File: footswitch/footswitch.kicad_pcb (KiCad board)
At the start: 2 copper layers, 100 x 50 mm, 65 parts, among them J1 control, Q1 TD9944, Q2 TD9944, Q3 TD9944, Q4 TD9944, SW1 SPST, SW2 SPST, SW3 SPST, U1 Teensy_LC, U2 74HC14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

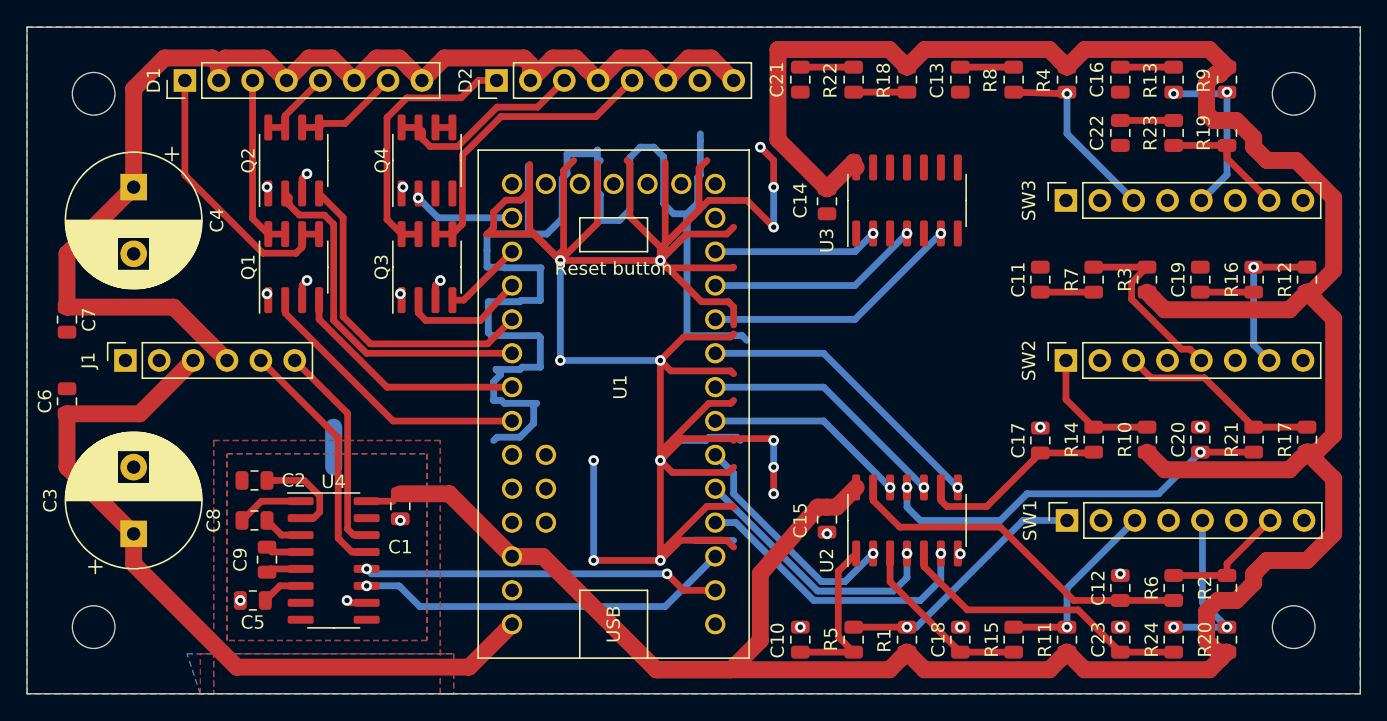
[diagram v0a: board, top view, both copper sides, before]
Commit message: Finalisation du PCB de la footswitch. Correction de la position des mounting holes.
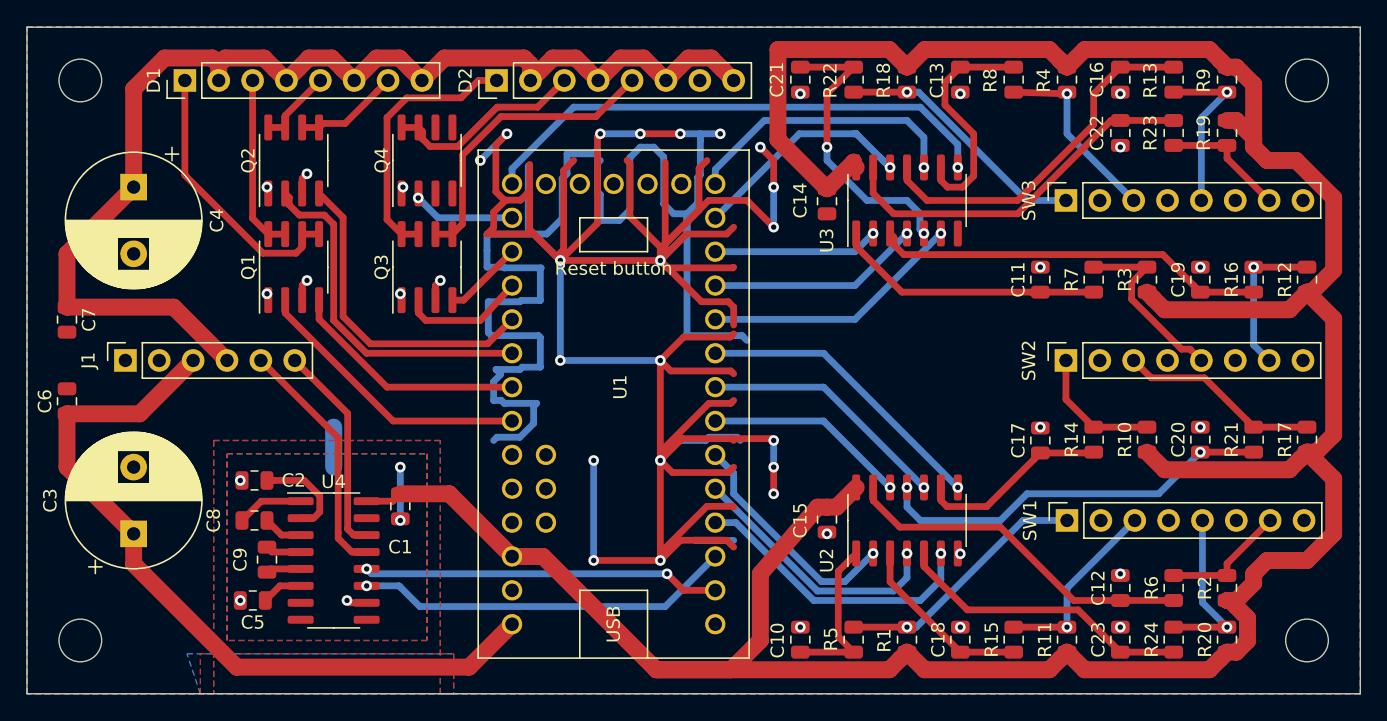
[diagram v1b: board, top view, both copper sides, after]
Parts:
- moved REF** 1.41 mm to (116.0, 66.0)
- moved REF** 1.41 mm to (116.0, 24.0)
- moved REF** 1.41 mm to (24.0, 24.0)
- moved REF** 1.41 mm to (24.0, 66.0)
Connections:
- U1 pad 11: /MCU_switchs/opt_3_sw -> /MCU_switchs/opt_5_sw
- U1 pad 13: /MCU_switchs/opt_5_sw -> /MCU_switchs/opt_3_sw
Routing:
- net /MCU_switchs/opt_3_sw: track 0.00 -> 39.4 mm, vias 0 -> 1
- net Net-(C19-Pad1): track 4.00 -> 29.4 mm
- net GNDD: track 325.0 -> 349.4 mm, vias 32 -> 46
- net Net-(C22-Pad1): track 4.00 -> 28.0 mm
- net Net-(C16-Pad1): track 4.00 -> 27.1 mm
- net /MCU_switchs/opt_4_sw: track 0.00 -> 21.0 mm, vias 0 -> 1
- net Net-(C21-Pad1): track 4.00 -> 22.1 mm, vias 0 -> 2
- net /MCU_switchs/opt_5_sw: track 0.00 -> 18.0 mm, vias 0 -> 1
- net Net-(C11-Pad1): track 4.00 -> 20.2 mm
- net Net-(R18-Pad2): track 4.00 -> 19.3 mm, vias 0 -> 1
- net Net-(C13-Pad1): track 4.00 -> 17.5 mm
- net (no net): track 1.27 -> 0.00 mm
- net /3V3: track 237.1 -> 238.0 mm
- net Net-(R13-Pad2): track 13.1 -> 12.9 mm, vias 2 -> 1
- net Net-(R20-Pad2): vias 2 -> 1

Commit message: Ajout des gerber pour control et footswitch.
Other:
- board text added: "- + clip/mute/comp/overdrive"
- board text added: "12V"
- board text added: "5V"
- board text added: "G"
- board text added: "RX"
- board text added: "TX"
- board text added: "delay/delay tap/reverb/opt1"
- board text added: "mute/comp/overdrive/octaver"
- board text added: "octaver/delay/reverb/power"
- board text added: "opt2/opt3/opt4/opt5"
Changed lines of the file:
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@@
   (general
     (thickness 1.6)
-    (drawings 4)
+    (drawings 15)
     (tracks 647)
     (zones 0)
@@
     (pcbplotparams
       (layerselection 0x010fc_ffffffff)
-      (usegerberextensions false)
+      (usegerberextensions true)
       (usegerberattributes false)
       (usegerberadvancedattributes false)
@@
       (outputformat 1)
       (mirror false)
-      (drillshape 1)
+      (drillshape 0)
       (scaleselection 1)
-      (outputdirectory ""))
+      (outputdirectory "berber"))
   )
   (net 0 "")
@@
     )
   )
+  (gr_text octaver/delay/reverb/power (at 65.5 21) (layer F.SilkS)
+    (effects (font (size 1 1) (thickness 0.15)))
+  )
+  (gr_text "- + clip/mute/comp/overdrive" (at 39 21) (layer F.SilkS)
+    (effects (font (size 1 1) (thickness 0.15)))
+  )
+  (gr_text opt2/opt3/opt4/opt5 (at 106.5 35.5) (layer F.SilkS)
+    (effects (font (size 1 1) (thickness 0.15)))
+  )
+  (gr_text "delay/delay tap/reverb/opt1" (at 106.5 47.5) (layer F.SilkS)
+    (effects (font (size 1 1) (thickness 0.15)))
+  )
+  (gr_text mute/comp/overdrive/octaver (at 106.5 59.5) (layer F.SilkS)
+    (effects (font (size 1 1) (thickness 0.15)))
+  )
+  (gr_text TX (at 40 48.5 90) (layer F.SilkS)
+    (effects (font (size 1 1) (thickness 0.15)))
+  )
+  (gr_text RX (at 37.5 48.5 90) (layer F.SilkS)
+    (effects (font (size 1 1) (thickness 0.15)))
+  )
+  (gr_text 12V (at 35 48.5 90) (layer F.SilkS)
+    (effects (font (size 1 1) (thickness 0.15)))
+  )
+  (gr_text 5V (at 32.5 48.5 90) (layer F.SilkS)
+    (effects (font (size 1 1) (thickness 0.15)))
+  )
+  (gr_text G (at 30 48.5 90) (layer F.SilkS)
+    (effects (font (size 1 1) (thickness 0.15)))
+  )
+  (gr_text G (at 27.5 48.5 90) (layer F.SilkS)
+    (effects (font (size 1 1) (thickness 0.15)))
+  )
   (gr_line (start 120 70) (end 20 70) (layer Edge.Cuts) (width 0.05))
